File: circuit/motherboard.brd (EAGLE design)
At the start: 100 x 80 mm, 3 parts

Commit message: Think I've got the circuitry down, boarding next
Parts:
- added R1: (no value), adafruit:0805-THM
- added S1, S2, S3, S4: (no value), switch-omron:B3F-10XX
- added S5: (no value), switch:255SB
- added T1: BC337, transistor:TO92
- added U$3: BATTERY-CHARGER-LI-PROT, diy-modules:BATTERY-CHARGER-LI-PROT
- moved U$2 49.3 mm to (35.6, 66.0), turned to 180 degrees
- moved DIS1 45.8 mm to (47.0, 58.4), turned to 180 degrees
- moved U$1 28.0 mm to (54.6, 47.0), turned to 90 degrees
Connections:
- removed net GND: DIS1.8
- removed net VCC: DIS1.6
- new net N$10: DIS1.4, U$1.D3
- new net N$11: DIS1.3, U$1.D4
- new net N$12: DIS1.2, U$1.D5
- new net N$13: DIS1.1, U$1.D7
- new net N$14: R1.1, U$1.D6
- new net N$15: S5.2, U$3.OUT+
- new net N$16: R1.2, T1.2
- new net N$17: DIS1.7, T1.3
- new net N$18: S4.1, S4.2, U$1.A0
- new net N$19: S3.1, S3.2, U$1.A1
- new net N$20: S2.1, S2.2, U$1.A2
- new net N$21: S1.1, S1.2, U$1.A3
- new net N$22: DIS1.8, S1.3, S2.3, S3.3, S4.3, U$1.GND, U$3.OUT-
- new net N$23: S5.3, U$1.5V
- new net N$9: DIS1.5, U$1.D2
- net N$1: now also DIS1.6
- net N$3: now also T1.1

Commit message: PCB coming along nicely
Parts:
- removed DIS1: NOKIA5110, _LCD_Nokia5110:NOKIA5110
- removed S5: (no value), switch:255SB
- removed U$2: AI-THINKER_RA-01, LoRa_modules:AI-THINKER_RA-01
- added DIS2: NOKIA5110, _LCD_Nokia5110-minimal:NOKIA5110
- added JP1: (no value), pinhead:1X02/90
- added R2, R3: 10k, adafruit:0805-THM
- added U$4: AI-THINKER_RA-01, lora-ra-02-minimal-because-labels-fuckup-rotating:AI-THINKER_RA-01
- R1: value (none) -> 10k
- moved T1 6.48 mm to (61.0, 58.4)
- moved R1 3.81 mm to (63.5, 67.3)
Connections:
- removed net N$14: R1.1, U$1.D6
- removed net N$15: S5.2, U$3.OUT+
- removed net N$22: DIS1.8, S1.3, S2.3, S3.3, S4.3, U$1.GND, U$3.OUT-
- removed net N$23: S5.3, U$1.5V
- new net +3V3: DIS2.6, U$1.3.3V, U$4.P$3
- new net +5V: U$1.5V, U$3.OUT+
- new net GND: DIS2.8, JP1.2, R2.2, S1.3, S2.3, S3.3, S4.3, T1.1, U$1.GND1, U$4.P$16
- new net N$24: R2.1, R3.2, U$1.A7
- new net N$25: R3.1, U$3.B+
- net N$1: now also JP1.1, U$3.OUT-; no longer DIS1.6, U$1.3.3V, U$2.P$3
- net N$10: now also DIS2.4, U$1.D6; no longer DIS1.4, U$1.D3
- net N$11: now also DIS2.3, U$1.D5; no longer DIS1.3, U$1.D4
- net N$12: now also DIS2.2, U$1.D4; no longer DIS1.2, U$1.D5
- net N$13: now also R1.1, U$1.D3; no longer DIS1.1, U$1.D7
- net N$17: now also DIS2.7; no longer DIS1.7
- net N$2: now also U$4.P$12; no longer U$2.P$12
- net N$3: now also DIS2.5, U$1.D7; no longer T1.1, U$1.GND1, U$2.P$16
- net N$4: now also U$4.P$13; no longer U$2.P$13
- net N$5: now also U$4.P$14; no longer U$2.P$14
- net N$6: now also U$4.P$15; no longer U$2.P$15
- net N$7: now also U$4.P$5; no longer U$2.P$5
- net N$8: now also U$4.P$4; no longer U$2.P$4
- net N$9: now also DIS2.1; no longer DIS1.5
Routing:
- net +3V3: track 0.00 -> 79.8 mm
- net N$17: track 0.00 -> 38.3 mm
- net N$2: track 0.00 -> 34.2 mm
- net N$3: track 0.00 -> 29.8 mm
- net N$10: track 0.00 -> 28.4 mm
- net N$11: track 0.00 -> 26.1 mm
- net N$12: track 0.00 -> 25.0 mm
- net N$9: track 0.00 -> 24.0 mm
- net N$6: track 0.00 -> 20.9 mm
- net N$7: track 0.00 -> 20.6 mm
- net N$8: track 0.00 -> 17.2 mm
- net N$5: track 0.00 -> 11.6 mm
- added copper zone on layer 1, net GND
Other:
- board size 100 x 80 mm -> 64.4 x 80 mm

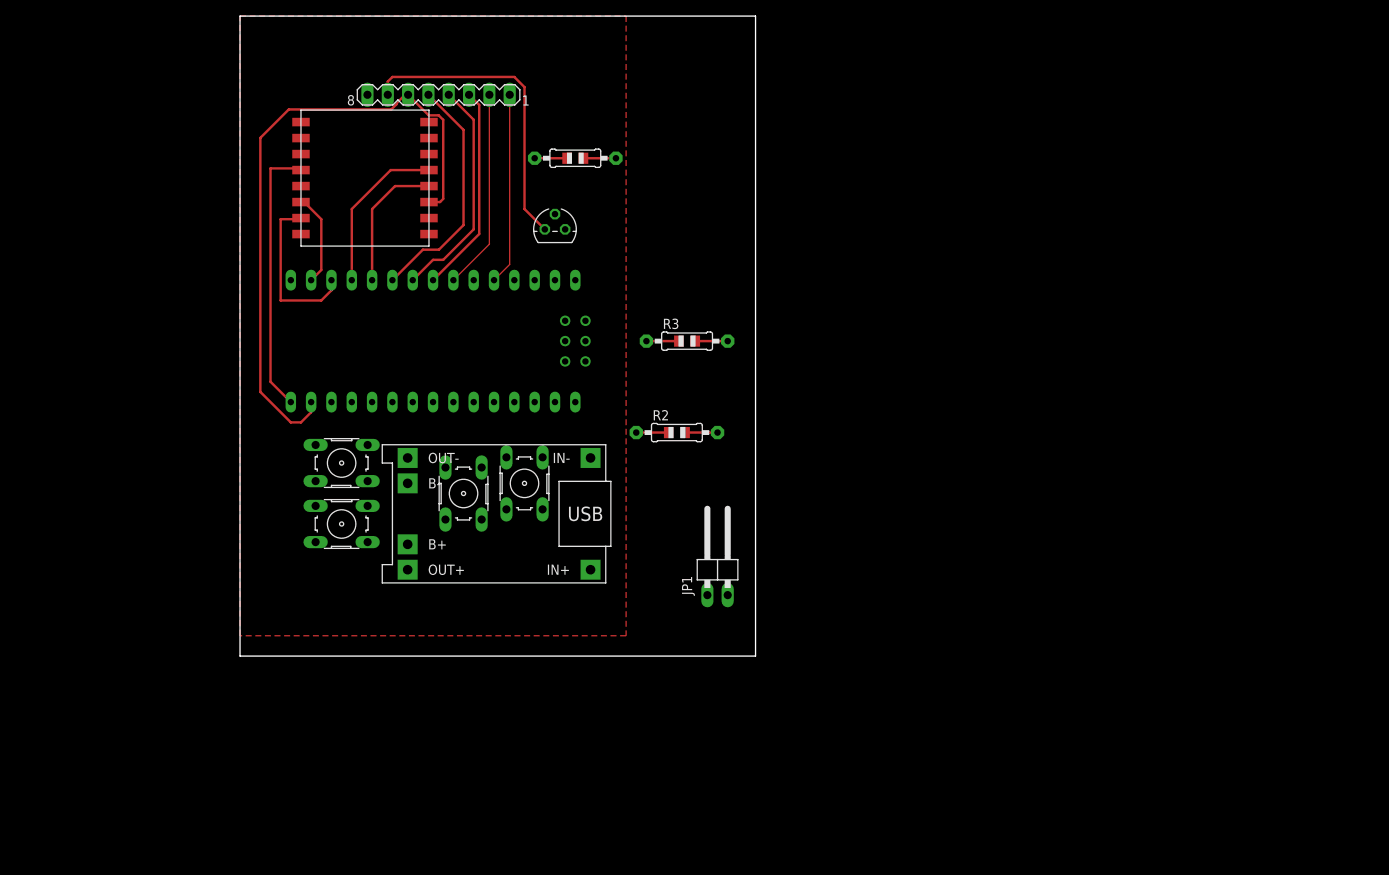
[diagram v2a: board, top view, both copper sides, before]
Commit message: Finished the PCB.. and then decided I should split the display/buttons separately
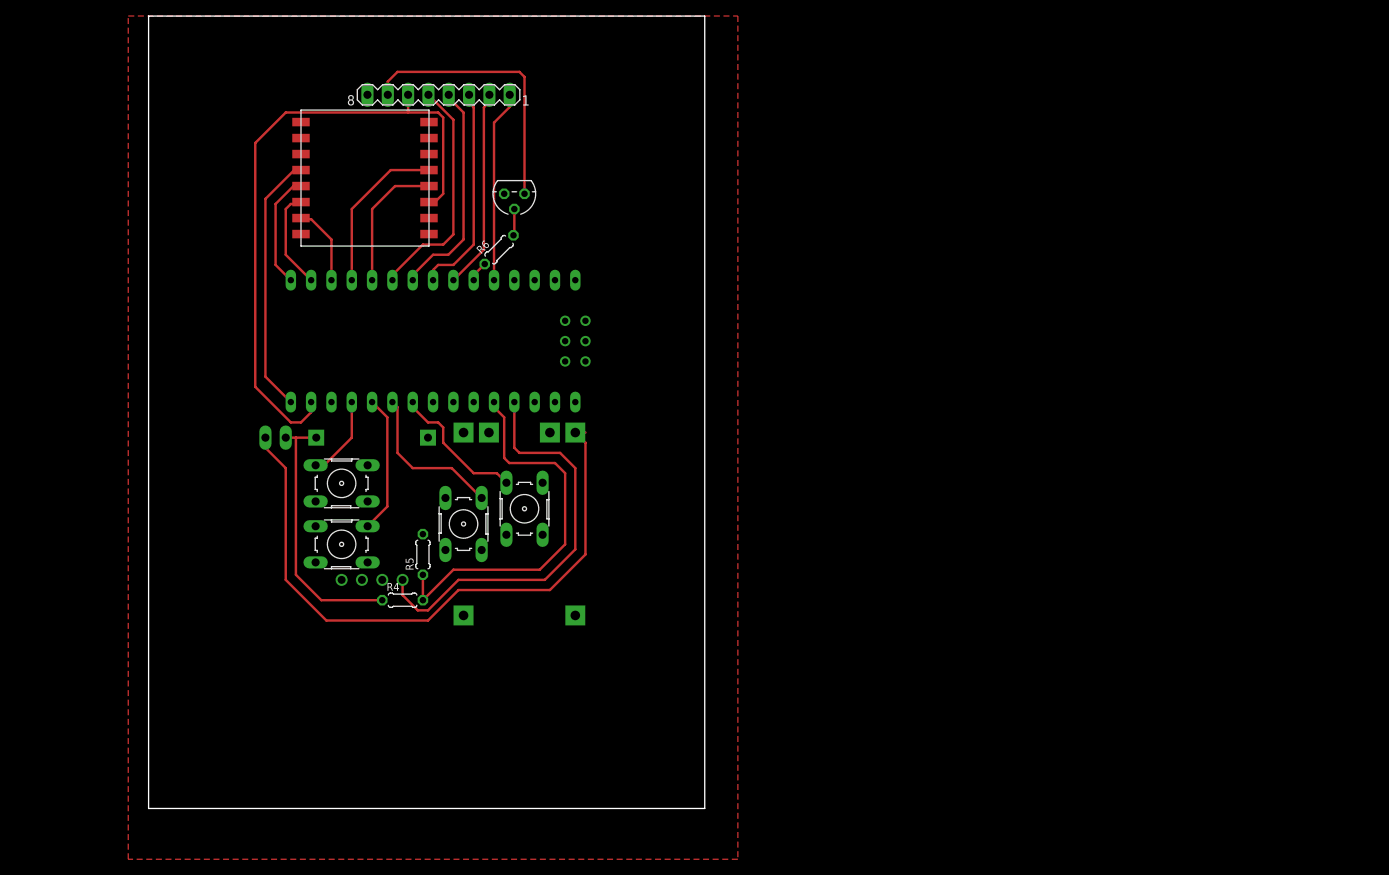
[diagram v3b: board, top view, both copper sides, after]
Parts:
- removed R1, R2, R3: 10k, adafruit:0805-THM
- added R4, R5, R6: 10k, rcl:0204/5
- added U$5: DC-DC-STEP-UP-5V, 5v-step-up-minimal:DC-DC-STEP-UP-5V
- moved JP1 56.5 mm to (26.0, 28.6), flipped to the bottom, turned to 180 degrees
- moved T1 6.75 mm to (55.9, 62.9), turned to 180 degrees
- moved S2 3.81 mm to (49.5, 21.6), turned to 270 degrees
- moved U$3 3.24 mm to (56.5, 22.2), flipped to the bottom, turned to 90 degrees
- moved S1 3.18 mm to (57.1, 23.5)
- moved S3 2.54 mm to (34.3, 19.1)
- moved S4 2.54 mm to (34.3, 26.7)
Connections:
- removed net N$25: R3.1, U$3.B+
- new net N$14: R6.2, T1.2
- new net N$15: JP1.1, U$3.OUT+
- net +5V: now also U$5.5V; no longer U$3.OUT+
- net GND: now also R5.2, U$5.GND, U$5.IN-; no longer JP1.2, R2.2
- net N$1: no longer JP1.1
- net N$13: now also R6.1; no longer R1.1
- net N$16: now also JP1.2, R4.1, U$5.IN+; no longer R1.2, T1.2
- net N$24: now also R4.2, R5.1; no longer R2.1, R3.2
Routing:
- net N$15: track 0.00 -> 78.9 mm
- net +5V: track 0.00 -> 52.0 mm
- net N$24: track 0.00 -> 48.7 mm
- net N$16: track 0.00 -> 33.1 mm
- net N$20: track 0.00 -> 19.5 mm
- net N$21: track 0.00 -> 17.4 mm
- net N$19: track 0.00 -> 17.3 mm
- net N$4: track 0.00 -> 14.4 mm
- net N$6: track 20.9 -> 10.0 mm
- net N$18: track 0.00 -> 10.4 mm
- net N$17: track 38.3 -> 34.1 mm
- net N$14: track 0.00 -> 3.33 mm
- net N$13: track 0.00 -> 2.59 mm
- net N$2: track 34.2 -> 32.7 mm
- net N$5: track 11.6 -> 12.9 mm
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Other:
- board size 64.4 x 80 mm -> 69.5 x 99 mm

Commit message: Getting to be quite a serious design..
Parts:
- added J1, J2: XF2L-2235-1, con-omron:XF2L-2235-1
- moved S2 51.6 mm to (101.0, 17.1)
- moved S3 45.7 mm to (79.4, 11.4)
- moved S4 44.4 mm to (78.1, 19.7)
- moved DIS2 43.7 mm to (86.4, 38.1)
- moved U$3 37.6 mm to (19.1, 19.1), flipped to the top
- moved S1 35.9 mm to (92.1, 15.2)
- moved JP1 33.6 mm to (13.3, 59.7), flipped to the top
- moved U$5 31.5 mm to (17.8, 45.7), flipped to the top, turned to 90 degrees
- moved R6 24.7 mm to (74.3, 41.9)
- moved T1 24.7 mm to (76.2, 48.9)
- moved U$1 19.8 mm to (39.4, 34.3), turned to 180 degrees
- moved R4 12.8 mm to (53.3, 6.35), turned to 90 degrees
- moved U$4 11.2 mm to (44.7, 56.5), turned to 0 degrees
- moved R5 9.94 mm to (53.3, 13.3)
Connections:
- removed net N$16: JP1.2, R4.1, U$5.IN+
- new net N$17: DIS2.1, J2.9
- new net N$22: J2.12, S3.3
- new net N$25: DIS2.6, J2.3
- new net N$26: DIS2.5, J2.4
- new net N$27: DIS2.4, J2.5
- new net N$28: DIS2.3, J2.6
- new net N$29: DIS2.2, J2.7
- new net N$30: J2.13, S4.3
- new net N$32: J1.13, U$1.A0
- new net N$33: J1.12, U$1.A1
- new net N$34: J1.11, U$1.A2
- new net N$35: J1.10, U$1.A3
- net +3V3: now also J1.20; no longer DIS2.6
- net GND: now also J1.22, J2.1, S1.1, S1.2, S2.1, S2.2, S3.1, S3.2, S4.1, S4.2; no longer S1.3, S2.3, S3.3, S4.3
- net N$10: now also J1.18; no longer DIS2.4
- net N$11: now also J1.17; no longer DIS2.3
- net N$12: now also J1.16; no longer DIS2.2
- net N$13: now also J1.15; no longer R6.1
- net N$15: now also JP1.2; no longer JP1.1
- net N$18: now also JP1.1, R4.1, U$5.IN+; no longer S4.1, S4.2, U$1.A0
- net N$19: now also J2.8, R6.1; no longer S3.1, S3.2, U$1.A1
- net N$20: now also J2.10, S1.3; no longer S2.1, S2.2, U$1.A2
- net N$21: now also J2.11, S2.3; no longer S1.1, S1.2, U$1.A3
- net N$3: now also J1.19; no longer DIS2.5
- net N$9: now also J1.14; no longer DIS2.1
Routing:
- net N$18: track 10.4 -> 95.9 mm
- net N$6: track 10.0 -> 83.0 mm
- net N$5: track 12.9 -> 77.7 mm
- net +3V3: track 80.4 -> 137.2 mm
- net N$32: track 0.00 -> 56.2 mm
- net N$4: track 14.4 -> 69.1 mm
- net N$33: track 0.00 -> 53.4 mm
- net N$34: track 0.00 -> 50.7 mm
- net N$35: track 0.00 -> 47.9 mm
- net N$15: track 78.9 -> 36.3 mm
- net N$23: track 34.1 -> 0.00 mm
- net N$16: track 33.1 -> 0.00 mm
- net N$13: track 2.59 -> 35.1 mm
- net N$24: track 48.7 -> 25.7 mm
- net +5V: track 52.0 -> 74.9 mm
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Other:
- board size 69.5 x 99 mm -> 155.2 x 104.8 mm

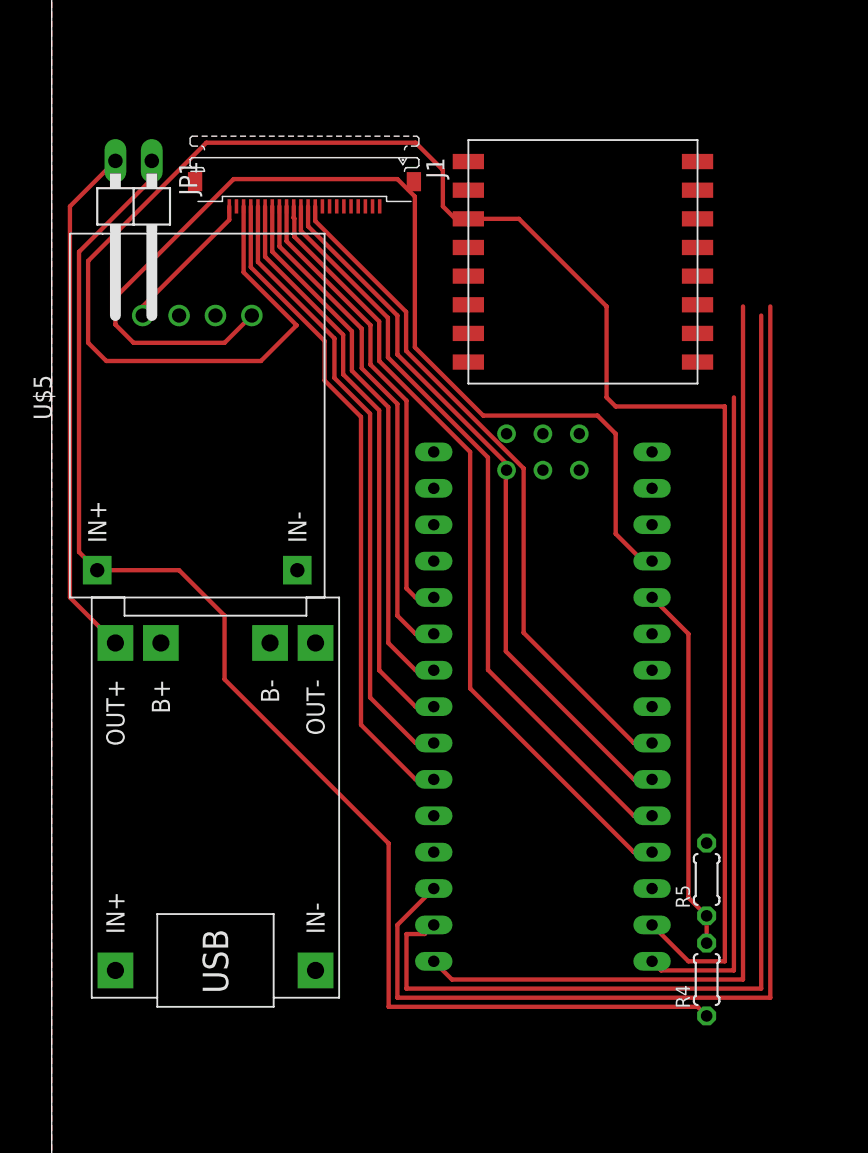
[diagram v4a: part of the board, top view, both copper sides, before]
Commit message: Library parts are annoying
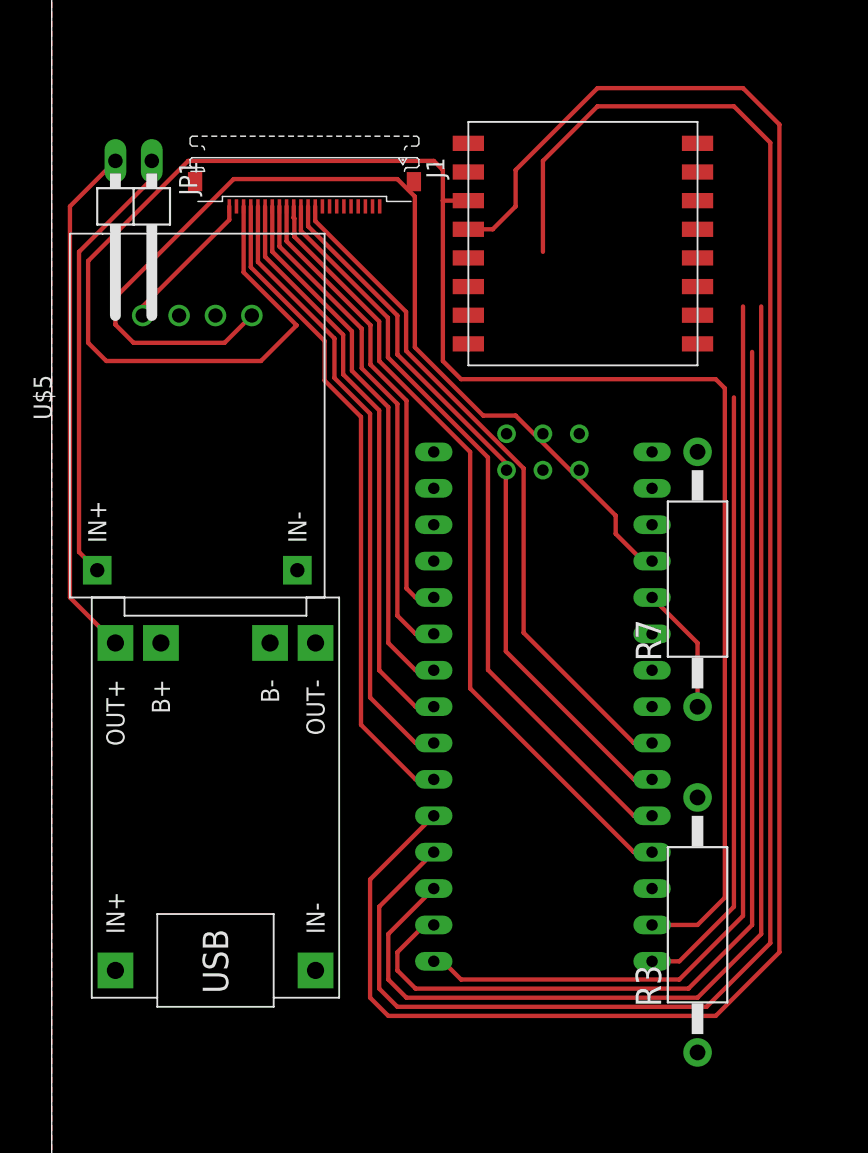
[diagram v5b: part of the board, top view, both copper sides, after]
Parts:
- removed R4, R5: 10k, rcl:0204/5
- added R3, R7: 10k, resistor-power:AC01
- moved U$4 1.27 mm to (44.7, 57.7)
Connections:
- removed net N$18: JP1.1, R4.1, U$5.IN+
- new net N$16: R3.1, U$3.B+
- net GND: now also R7.2, U$3.OUT-; no longer R5.2
- net N$1: now also JP1.1, U$5.IN+; no longer U$3.OUT-
- net N$24: now also R3.2, R7.1; no longer R4.2, R5.1
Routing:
- net N$8: track 0.00 -> 131.6 mm
- net N$7: track 0.00 -> 121.5 mm
- net N$18: track 95.9 -> 0.00 mm
- net N$1: track 0.00 -> 31.2 mm
- net N$24: track 25.7 -> 8.94 mm
- net N$5: track 77.7 -> 71.7 mm
- net +5V: track 74.9 -> 71.6 mm
- net N$2: track 46.0 -> 42.9 mm
- net N$6: track 83.0 -> 79.9 mm
- net N$4: track 69.1 -> 66.5 mm
- net +3V3: track 137.2 -> 136.6 mm

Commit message: Motherboard complete!
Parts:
- U$1: device Arduino-clone:NANO -> Arduino-clone-nano-minimal:NANO
- moved R3 0.63 mm to (52.7, 10.8)
- moved U$5 0.63 mm to (18.4, 45.7)
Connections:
- net GND: now also U$4.P$2
- net N$1: now also U$3.OUT+; no longer U$5.IN+
- net N$15: now also U$5.IN+; no longer U$3.OUT+
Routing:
- net N$16: track 0.00 -> 55.7 mm
- net N$5: track 71.7 -> 85.1 mm
- net N$6: track 79.9 -> 92.8 mm
- net N$2: track 42.9 -> 54.6 mm
- net N$4: track 66.5 -> 74.1 mm
- net N$15: track 36.3 -> 29.4 mm
- net +5V: track 71.6 -> 77.4 mm
- net N$1: track 31.2 -> 36.3 mm
- net +3V3: track 136.6 -> 133.2 mm
- net N$7: track 121.5 -> 124.4 mm
- net N$35: track 47.9 -> 49.8 mm
- net N$34: track 50.7 -> 52.6 mm
- net N$33: track 53.4 -> 55.3 mm
- net N$32: track 56.2 -> 58.1 mm
- net N$8: track 131.6 -> 130.0 mm

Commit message: Okay _now_ I'm happy with the motherboard
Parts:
- moved DIS2 32.5 mm to (88.9, 5.71)
- moved S3 6.35 mm to (73.0, 11.4)
- moved S4 5.24 mm to (73.0, 18.4)
- moved R3 4.07 mm to (55.2, 14.0), turned to 105 degrees
- moved S2 3.17 mm to (103.5, 15.2)
- moved J1 1.91 mm to (24.8, 64.1)
- moved S1 1.42 mm to (90.8, 14.6)
- moved U$5 1.27 mm to (19.7, 45.7)
- moved U$3 0.90 mm to (19.7, 18.4)
- moved J2 0.64 mm to (87.6, 3.81)
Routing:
- net N$35: track 49.8 -> 55.2 mm
- net N$34: track 52.6 -> 57.8 mm
- net N$33: track 55.3 -> 60.4 mm
- net N$32: track 58.1 -> 62.9 mm
- net N$16: track 55.7 -> 60.1 mm
- net N$9: track 32.3 -> 36.3 mm
- net N$13: track 35.1 -> 38.8 mm
- net +5V: track 77.4 -> 81.1 mm
- net N$12: track 37.8 -> 41.3 mm
- net +3V3: track 133.2 -> 136.6 mm
- net N$11: track 40.5 -> 43.8 mm
- net N$10: track 43.3 -> 46.3 mm
- net N$24: track 8.94 -> 11.9 mm
- net GND: track 9.86 -> 12.7 mm
- net N$3: track 46.0 -> 48.8 mm
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
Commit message: Real life is gritty! - Etching at this point
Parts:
- moved R6 31.3 mm to (83.8, 12.1), turned to 180 degrees
- moved T1 30.4 mm to (81.9, 19.1), turned to 90 degrees
- moved S2 29.5 mm to (74.3, 19.1), turned to 180 degrees
- moved S4 28.6 mm to (101.6, 17.8), turned to 90 degrees
- moved S3 21.6 mm to (94.0, 16.5), turned to 90 degrees
- moved S1 16.7 mm to (74.3, 12.1), turned to 180 degrees
- moved R3 4.45 mm to (59.7, 14.0)
- moved R7 4.45 mm to (57.1, 34.3)
- moved J2 3.18 mm to (87.6, 6.99)
- moved U$4 2.54 mm to (47.2, 57.7)
- moved U$1 1.91 mm to (41.3, 34.3)
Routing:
- net N$21: track 0.00 -> 28.4 mm
- net N$17: track 0.00 -> 26.4 mm
- net N$29: track 0.00 -> 22.7 mm
- net N$28: track 0.00 -> 21.3 mm
- net N$30: track 0.00 -> 18.8 mm
- net N$26: track 0.00 -> 17.7 mm
- net N$27: track 0.00 -> 17.3 mm
- net N$25: track 0.00 -> 15.6 mm
- net N$20: track 0.00 -> 15.3 mm
- net GND: track 12.7 -> 0.00 mm
- net N$22: track 0.00 -> 11.4 mm
- net +5V: track 81.1 -> 71.3 mm
- net N$14: track 0.00 -> 7.51 mm
- net N$6: track 92.4 -> 99.7 mm
- net N$5: track 84.8 -> 92.1 mm
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- added copper zone on layer 1, net N$18
- added copper zone on layer 1, net N$31
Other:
- board size 155.2 x 104.8 mm -> 110.8 x 69.2 mm
